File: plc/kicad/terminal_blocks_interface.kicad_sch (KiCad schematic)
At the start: 80 parts, among them CN1 DB128V-5.08-2P-GN-S, CN10 DB128V-5.08-2P-GN-S, CN13 DB128V-5.08-2P-GN-S, CN14 DB128V-5.08-2P-GN-S, CN2 DB128V-5.08-2P-GN-S, CN3 DB128V-5.08-2P-GN-S, CN4 DB128V-5.08-2P-GN-S, CN5 DB128V-5.08-2P-GN-S, CN6 DB128V-5.08-2P-GN-S, CN7 DB128V-5.08-2P-GN-S, CN8 DB128V-5.08-2P-GN-S, CN9 DB128V-5.08-2P-GN-S, Q1 AO3400A, Q2 AO3400A, U1 TCA9535PWR, U2 TPS272C45DRHFR, U3 TPS272C45DRHFR, U4 ADS1115IDGSR, U5 LTV-814S-TA1-A, U6 LTV-814S-TA1-A, U7 LTV-814S-TA1-A, U8 LTV-814S-TA1-A

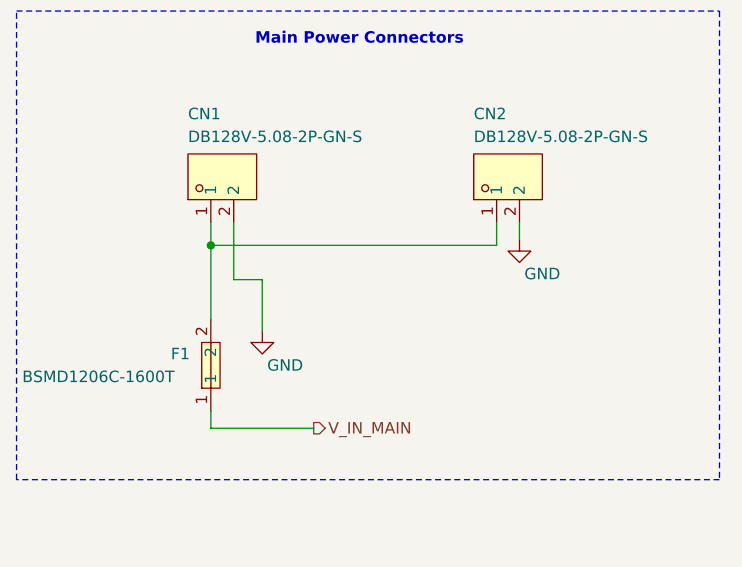
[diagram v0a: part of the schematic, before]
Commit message: Changed CAN & RS485 to input voltage unprotected
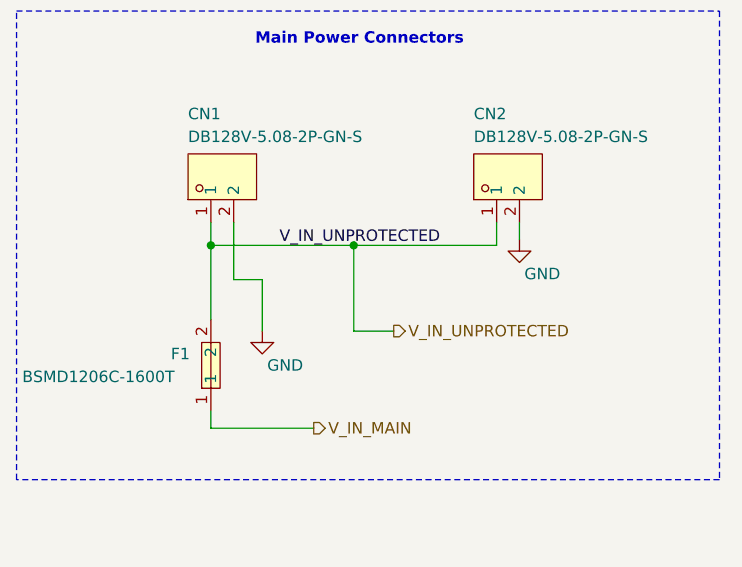
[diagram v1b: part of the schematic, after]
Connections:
- net V_IN_UNPROTECTED: now reaches CN1.1, CN2.1, F1.2
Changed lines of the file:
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@@
 	)
 	(junction
+		(at 358.775 223.52)
+		(diameter 0)
+		(color 0 0 0 0)
+	)
+	(junction
 		(at 172.212 57.912)
 		(diameter 0)
@@
 	(wire
 		(pts
+			(xy 358.775 223.52) (xy 374.65 223.52)
+		)
+		(stroke
+			(width 0)
+			(type default)
+		)
+	)
+	(wire
+		(pts
 			(xy 38.989 159.512) (xy 42.799 159.512)
 		)
@@
 	(wire
 		(pts
+			(xy 363.22 233.045) (xy 358.775 233.045)
+		)
+		(stroke
+			(width 0)
+			(type default)
+		)
+	)
+	(wire
+		(pts
 			(xy 105.156 211.455) (xy 104.14 211.455)
 		)
@@
 	(wire
 		(pts
+			(xy 358.775 233.045) (xy 358.775 223.52)
+		)
+		(stroke
+			(width 0)
+			(type default)
+		)
+	)
+	(wire
+		(pts
 			(xy 72.644 267.081) (xy 72.644 268.351)
 		)
@@
 	(wire
 		(pts
-			(xy 342.9 223.52) (xy 374.65 223.52)
+			(xy 342.9 223.52) (xy 358.775 223.52)
 		)
 		(stroke
@@
 		)
 	)
+	(label "V_IN_UNPROTECTED"
+		(at 350.52 223.52 0)
+		(effects
+			(font
+				(size 1.27 1.27)
+			)
+			(justify left bottom)
+		)
+	)
 	(label "T2_ILIM2"
 		(at 45.339 191.897 180)
@@
 		)
 	)
+	(hierarchical_label "V_IN_UNPROTECTED"
+		(shape output)
+		(at 363.22 233.045 0)
+		(effects
+			(font
+				(size 1.27 1.27)
+			)
+			(justify left)
+		)
+	)

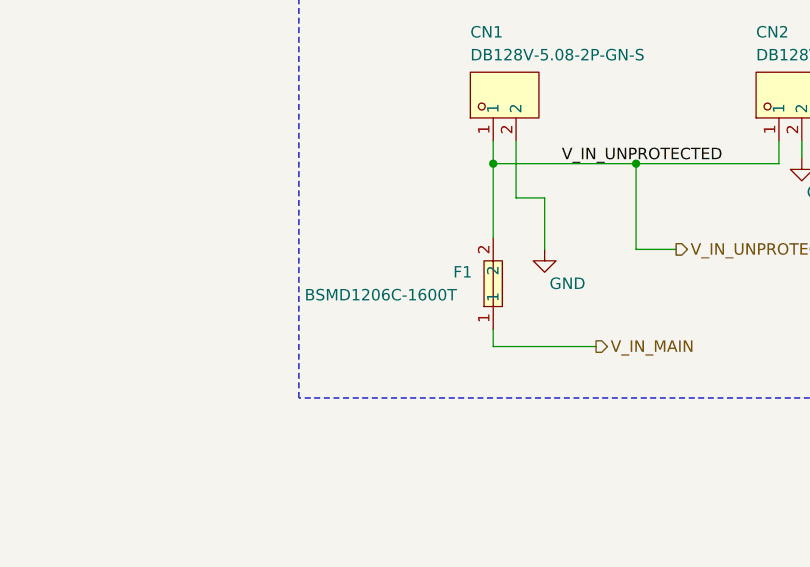
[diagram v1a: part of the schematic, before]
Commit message: Updated SMD fuses to fuse holders
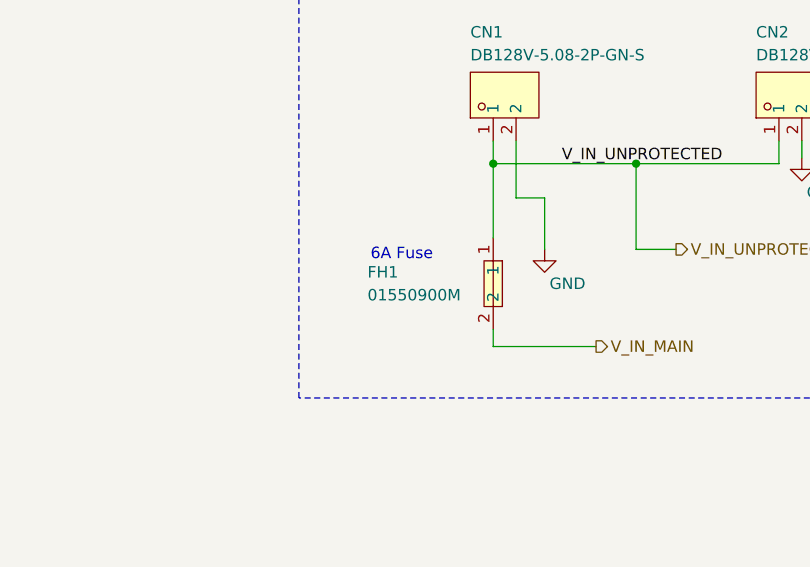
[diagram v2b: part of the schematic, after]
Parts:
- removed F1: BSMD1206C-1600T, LibrePLC32:F1206, symbol LibrePLC32:BSMD1206C-1600T
- added FH1: 01550900M, LibrePLC32:FUSE-SMD_L9.8-W5.0_01550900M, symbol LibrePLC32:01550900M
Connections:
- net V_IN_MAIN: now also FH1.2
- net V_IN_UNPROTECTED: now also FH1.1
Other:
- note added: "6A Fuse"
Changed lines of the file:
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@@
 		)
 	)
+	(text "6A Fuse"
+		(exclude_from_sim no)
+		(at 332.74 233.68 0)
+		(effects
+			(font
+				(size 1.27 1.27)
+			)
+		)
+	)
 	(text "\nNO\n\nCOM"
 		(exclude_from_sim no)
@@
 		(length 2.54)
 		(shape round)
-		(at 340.995 232.41 90)
+		(at 340.995 230.505 90)
 		(effects
 			(font
@@
 		)
 		(property "Net Class" "SYS_HV"
-			(at 330.2 232.41 0)
+			(at 330.2 230.505 0)
 			(show_name no)
 			(do_not_autoplace no)
@@
 		)
 		(property "Component Class" ""
-			(at 362.585 317.5 0)
+			(at 362.585 315.595 0)
 			(show_name no)
 			(do_not_autoplace no)
@@
 	)
 	(symbol
-		(lib_id "LibrePLC32:BSMD1206C-1600T")
-		(at 342.9 236.855 90)
-		(unit 1)
-		(body_style 1)
-		(exclude_from_sim no)
-		(in_bom yes)
-		(on_board yes)
-		(in_pos_files yes)
-		(dnp no)
-		(property "Reference" "F1"
-			(at 338.455 235.585 90)
-			(show_name no)
-			(do_not_autoplace no)
-			(effects
-				(font
-					(size 1.27 1.27)
-				)
-				(justify right)
-			)
-		)
-		(property "Value" "BSMD1206C-1600T"
-			(at 321.945 238.125 90)
-			(show_name no)
-			(do_not_autoplace no)
-			(effects
-				(font
-					(size 1.27 1.27)
-				)
-				(justify right)
-			)
-		)
-		(property "Footprint" "LibrePLC32:F1206"
-			(at 350.52 236.855 0)
-			(hide yes)
-			(show_name no)
-			(do_not_autoplace no)
-			(effects
-				(font
-					(size 1.27 1.27)
-				)
-			)
-		)
-		(property "Datasheet" "https://www.lcsc.com/datasheet/C49328461.pdf"
-			(at 353.06 236.855 0)
-			(hide yes)
-			(show_name no)
-			(do_not_autoplace no)
-			(effects
-				(font
-					(size 1.27 1.27)
-				)
-			)
-		)
-		(property "Description" ""
-			(at 342.9 236.855 0)
-			(hide yes)
-			(show_name no)
-			(do_not_autoplace no)
-			(effects
-				(font
-					(size 1.27 1.27)
-				)
-			)
-		)
-		(property "Manufacturer" "BHFUSE(佰宏)"
-			(at 355.6 236.855 0)
-			(hide yes)
-			(show_name no)
-			(do_not_autoplace no)
-			(effects
-				(font
-					(size 1.27 1.27)
-				)
-			)
-		)
-		(property "MPN" "BSMD1206C-1600T"
-			(at 358.14 236.855 0)
-			(hide yes)
-			(show_name no)
-			(do_not_autoplace no)
-			(effects
-				(font
-					(size 1.27 1.27)
-				)
-			)
-		)
-		(property "LCSC Part" "C49328461"
-			(at 360.68 236.855 0)
-			(hide yes)
-			(show_name no)
-			(do_not_autoplace no)
-			(effects
-				(font
-					(size 1.27 1.27)
-				)
-			)
-		)
-		(pin "1"
-		)
-		(pin "2"
-		)
-		(instances
-			(project "LibrePLC32"
-				(path "/ef4c1a27-85a3-413a-9f93-a41c4f97eee5/7299de7e-bdc9-4cc1-ab0f-f2b9af304cf6"
-					(reference "F1")
-					(unit 1)
-				)
-			)
-		)
-	)
-	(symbol
 		(lib_id "Device:R")
 		(at 172.212 91.567 180)
@@
 					(unit 1)
 				)
+			)
+		)
+	)
+	(symbol
+		(lib_id "LibrePLC32:01550900M")
+		(at 342.9 236.855 270)
+		(unit 1)
+		(body_style 1)
+		(exclude_from_sim no)
+		(in_bom yes)
+		(on_board yes)
+		(in_pos_files yes)
+		(dnp no)
+		(property "Reference" "FH1"
+			(at 328.93 235.585 90)
+			(show_name no)
+			(do_not_autoplace no)
+			(effects
+				(font
+					(size 1.27 1.27)
+				)
+				(justify left)
+			)
+		)
+		(property "Value" "01550900M"
+			(at 328.93 238.125 90)
+			(show_name no)
+			(do_not_autoplace no)
+			(effects
+				(font
+					(size 1.27 1.27)
+				)
+				(justify left)
+			)
+		)
+		(property "Footprint" "LibrePLC32:FUSE-SMD_L9.8-W5.0_01550900M"
+			(at 335.28 236.855 0)
+			(hide yes)
+			(show_name no)
+			(do_not_autoplace no)
+			(effects
+				(font
+					(size 1.27 1.27)
+				)
+			)
+		)
+		(property "Datasheet" "https://lcsc.com/product-detail/Others_Littelfuse_01550900M_Littelfuse-01550900M_C108518.html"
+			(at 332.74 236.855 0)
+			(hide yes)
+			(show_name no)
+			(do_not_autoplace no)
+			(effects
+				(font
+					(size 1.27 1.27)
+				)
+			)
+		)
+		(property "Description" ""
+			(at 342.9 236.855 0)
+			(hide yes)
+			(show_name no)
+			(do_not_autoplace no)
+			(effects
+				(font
+					(size 1.27 1.27)
+				)
+			)
+		)
+		(property "Manufacturer" "Littelfuse(美国力特)"
+			(at 330.2 236.855 0)
+			(hide yes)
+			(show_name no)
+			(do_not_autoplace no)
+			(effects
+				(font
+					(size 1.27 1.27)
+				)
+			)
+		)
+		(property "MPN" "01550900M"
+			(at 327.66 236.855 0)
+			(hide yes)
+			(show_name no)
+			(do_not_autoplace no)
+			(effects
+				(font
+					(size 1.27 1.27)
+				)
+			)
+		)
+		(property "LCSC Part" "C108518"
+			(at 325.12 236.855 0)
+			(hide yes)
+			(show_name no)
+			(do_not_autoplace no)
+			(effects
+				(font
+					(size 1.27 1.27)
+				)
+			)
+		)
+		(pin "2"
+		)
+		(pin "1"
+		)
+		(instances
+			(project "LibrePLC32"
+				(path "/ef4c1a27-85a3-413a-9f93-a41c4f97eee5/7299de7e-bdc9-4cc1-ab0f-f2b9af304cf6"
+					(reference "FH1")
+					(unit 1)
+				)

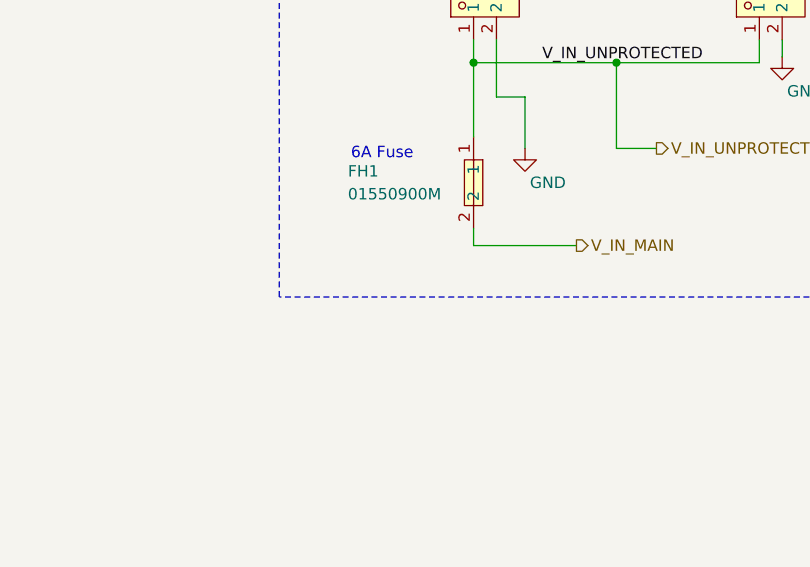
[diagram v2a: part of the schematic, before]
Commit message: Added fuse info
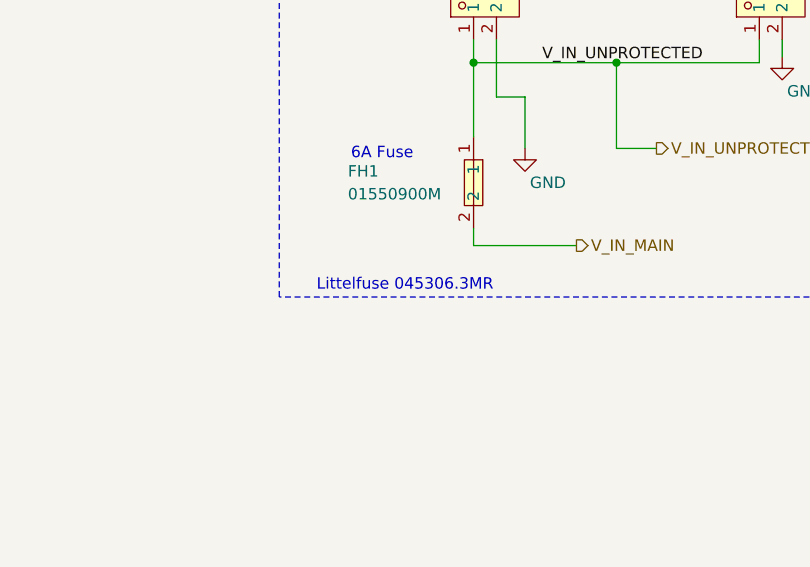
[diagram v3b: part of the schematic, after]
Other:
- note added: "Littelfuse 045306.3MR"
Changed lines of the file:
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@@
+		)
+	)
+	(text "Littelfuse 045306.3MR"
+		(exclude_from_sim no)
+		(at 335.28 248.285 0)
+		(effects
+			(font
+				(size 1.27 1.27)
+			)
 		)
 	)
